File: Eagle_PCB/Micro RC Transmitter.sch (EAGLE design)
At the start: 34 parts, among them IC1 NRF24L01+, Q1 BC337-25, U1 JOYSTICKPTH, U2 JOYSTICKPTH, U3 ARDUINO_PRO_MINI, U4 0.96"_I2C_OLED2

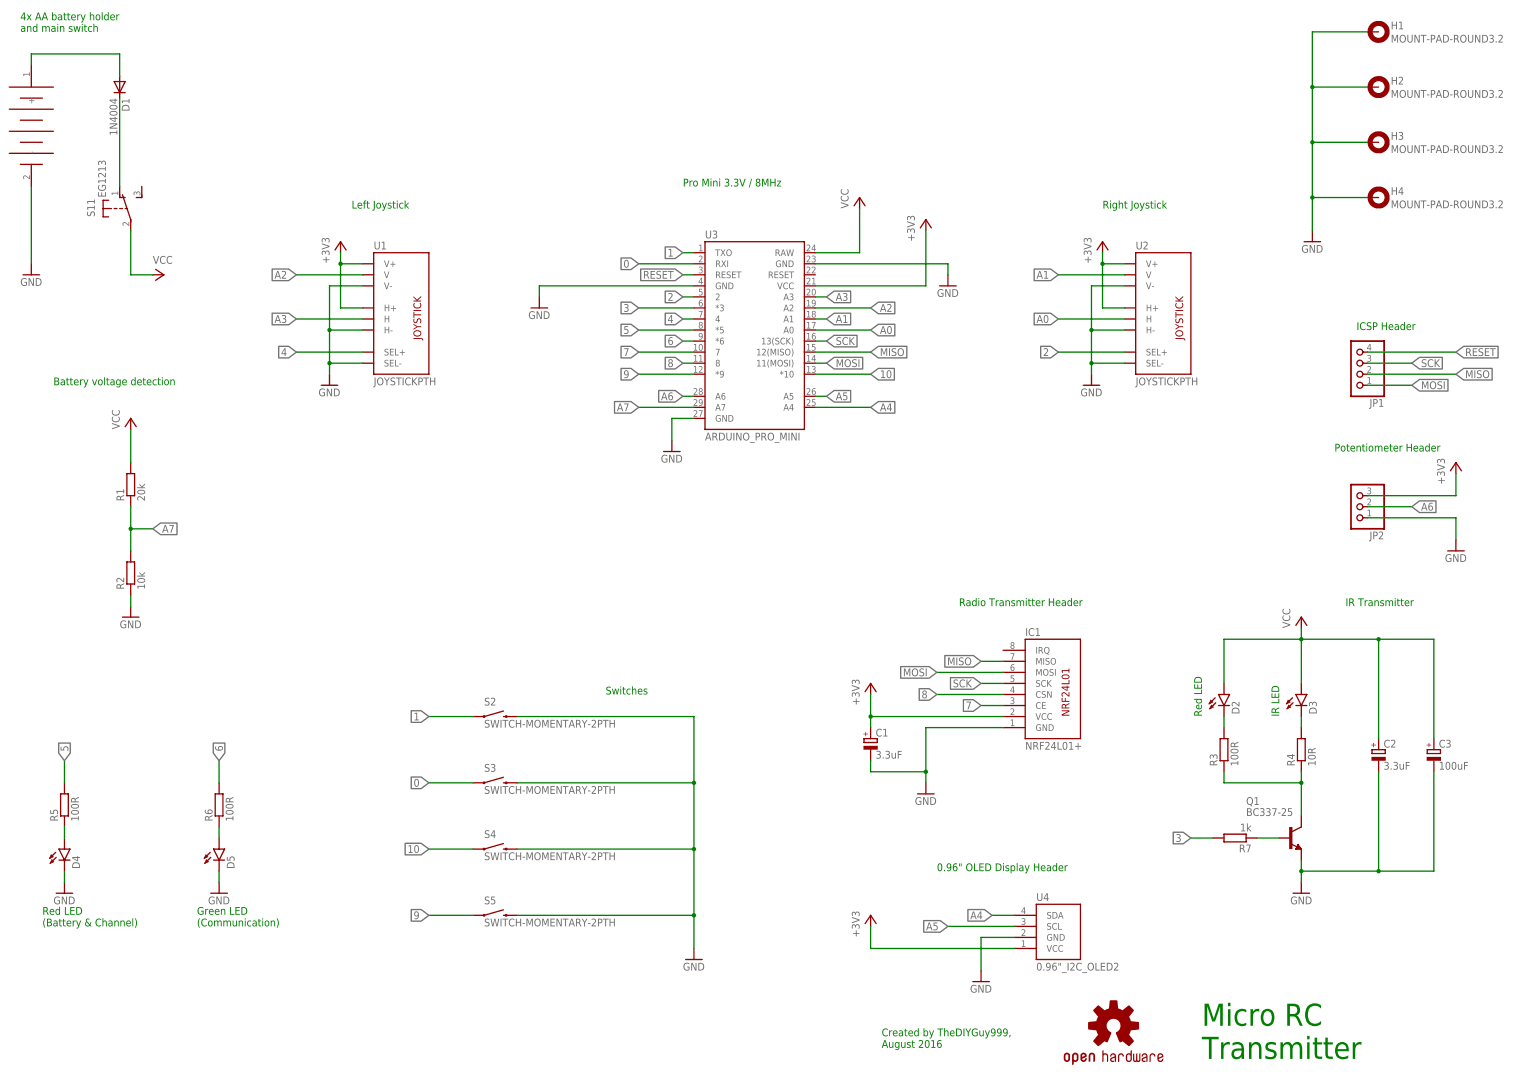
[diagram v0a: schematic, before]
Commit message: New board revision 1.2
separate voltage regulator for NRF24L01 radio transmitter. Allows to use a a model with power amplifier.
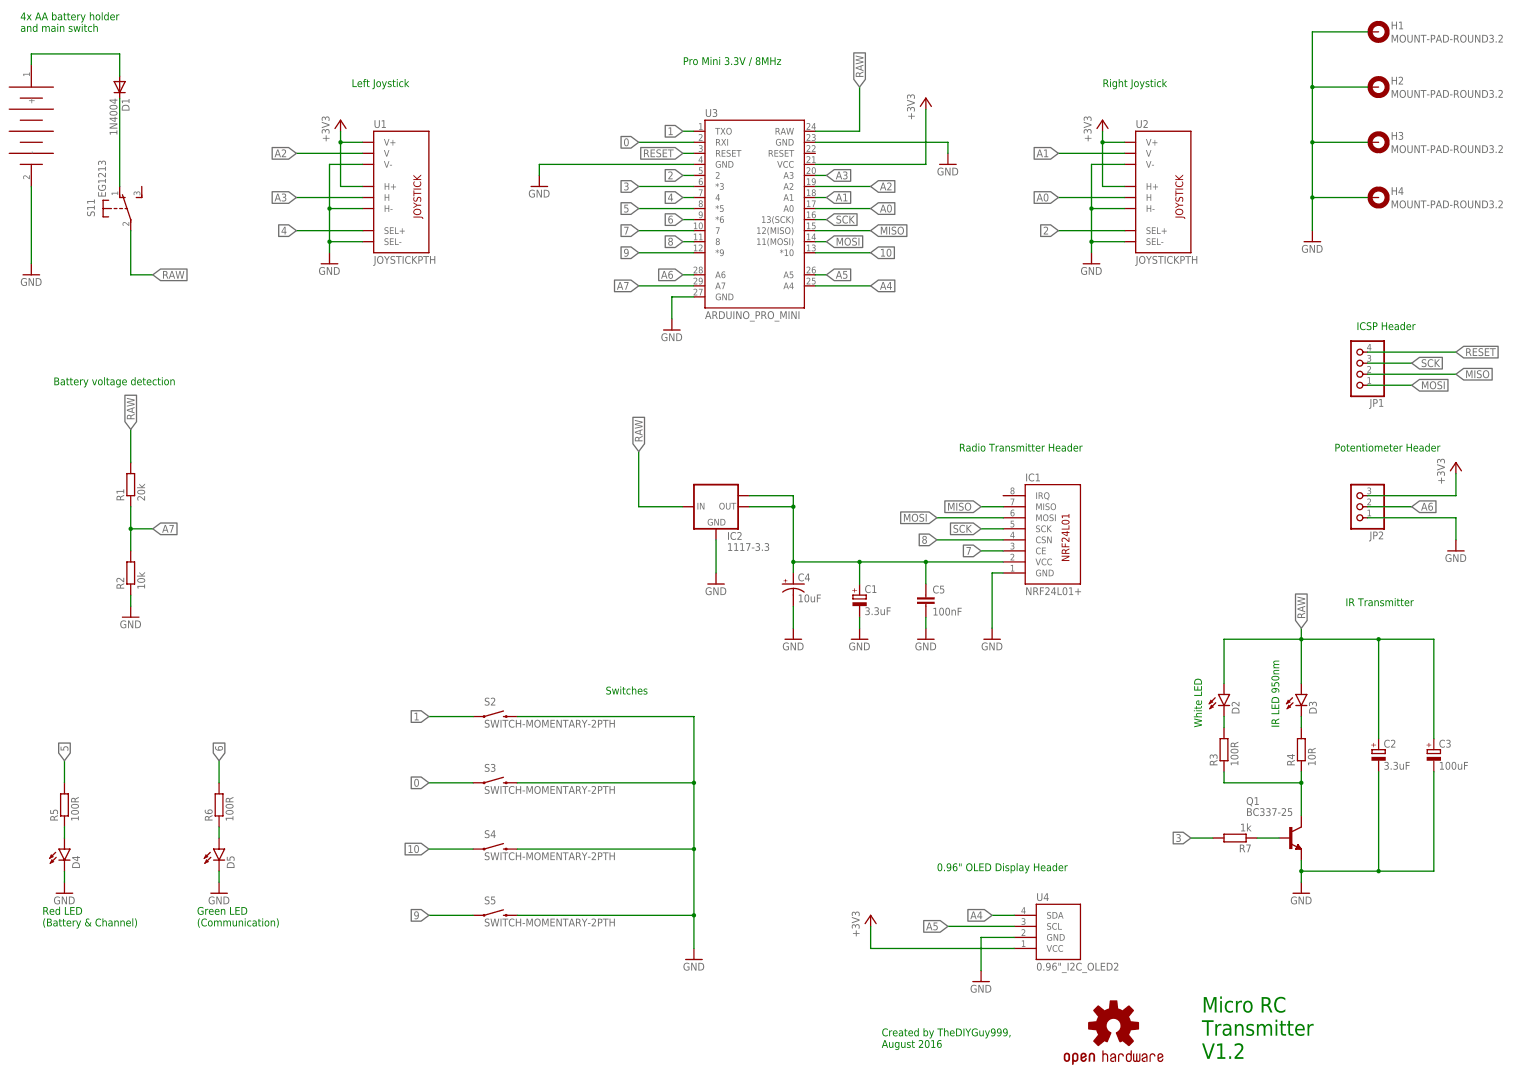
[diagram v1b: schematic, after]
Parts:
- added C4: 10uF, SparkFun-Capacitors:10UF-16V-10%(TANT)
- added C5: 100nF, rcl:C-EUC0805
- added IC2: 1117-3.3, lm1117:LM1117MPX-3.3
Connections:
- removed net VCC: C2.+, C3.+, D2.A, D3.A, R1.2, S11.P, U3.RAW
- new net N$9: C1.+, C4.+, C5.1, IC1.VCC, IC2.OUT, IC2.OUT1
- new net RAW: C2.+, C3.+, D2.A, D3.A, IC2.IN, R1.2, S11.P, U3.RAW
- net +3V3: no longer C1.+, IC1.VCC
- net GND: now also C4.-, C5.2, IC2.GND
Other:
- note added: "IR LED 950nm"
- note added: "Micro RC Transmitter V1.2"
- note added: "White LED"
- note removed: "IR LED"
- note removed: "Micro RC Transmitter"
- note removed: "Red LED"
- moved on the sheet: C1, IC1, U1, U2, U3

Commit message: LED resistor values increased
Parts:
- R3, R5, R6: value 100R -> 150R
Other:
- note added: "IR LED 950nm TSAL6200"
- note removed: "IR LED 950nm"
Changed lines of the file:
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@@
 <part name="D4" library="SparkFun-LED" deviceset="LED" device="3MM"/>
 <part name="D5" library="SparkFun-LED" deviceset="LED" device="3MM"/>
-<part name="R5" library="rcl" deviceset="R-EU_" device="0207/10" value="100R"/>
-<part name="R6" library="rcl" deviceset="R-EU_" device="0207/10" value="100R"/>
+<part name="R5" library="rcl" deviceset="R-EU_" device="0207/10" value="150R"/>
+<part name="R6" library="rcl" deviceset="R-EU_" device="0207/10" value="150R"/>
 <part name="GND11" library="supply1" deviceset="GND" device=""/>
 <part name="GND12" library="supply1" deviceset="GND" device=""/>
@@
 <part name="D2" library="SparkFun-LED" deviceset="LED" device="5MM"/>
 <part name="D1" library="diode" deviceset="1N4004" device=""/>
-<part name="R3" library="rcl" deviceset="R-EU_" device="0207/10" value="100R"/>
+<part name="R3" library="rcl" deviceset="R-EU_" device="0207/10" value="150R"/>
 <part name="R4" library="rcl" deviceset="R-EU_" device="0207/10" value="10R"/>
 <part name="R1" library="rcl" deviceset="R-EU_" device="0207/10" value="20k"/>
@@
 V1.2</text>
 <text x="294.64" y="83.82" size="1.778" layer="91" rot="R90">White LED</text>
-<text x="312.42" y="83.82" size="1.778" layer="91" rot="R90">IR LED 950nm</text>
+<text x="312.42" y="83.82" size="1.778" layer="91" rot="R90">IR LED 950nm
+TSAL6200</text>
 <text x="327.66" y="111.76" size="1.778" layer="91">IR Transmitter</text>
 <text x="238.76" y="147.32" size="1.778" layer="91">Radio Transmitter Header</text>
